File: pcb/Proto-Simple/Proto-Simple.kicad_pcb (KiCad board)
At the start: 2 copper layers, 52 x 63 mm, 341 parts, among them J1 Conn_01x04, J10 Conn_01x01, J11 Conn_01x01, J12 Conn_01x01, J13 Conn_01x01, J14 Conn_01x01, J2 Conn_01x01, J3 Conn_01x01, J4 Conn_01x01, J41 Conn_01x01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

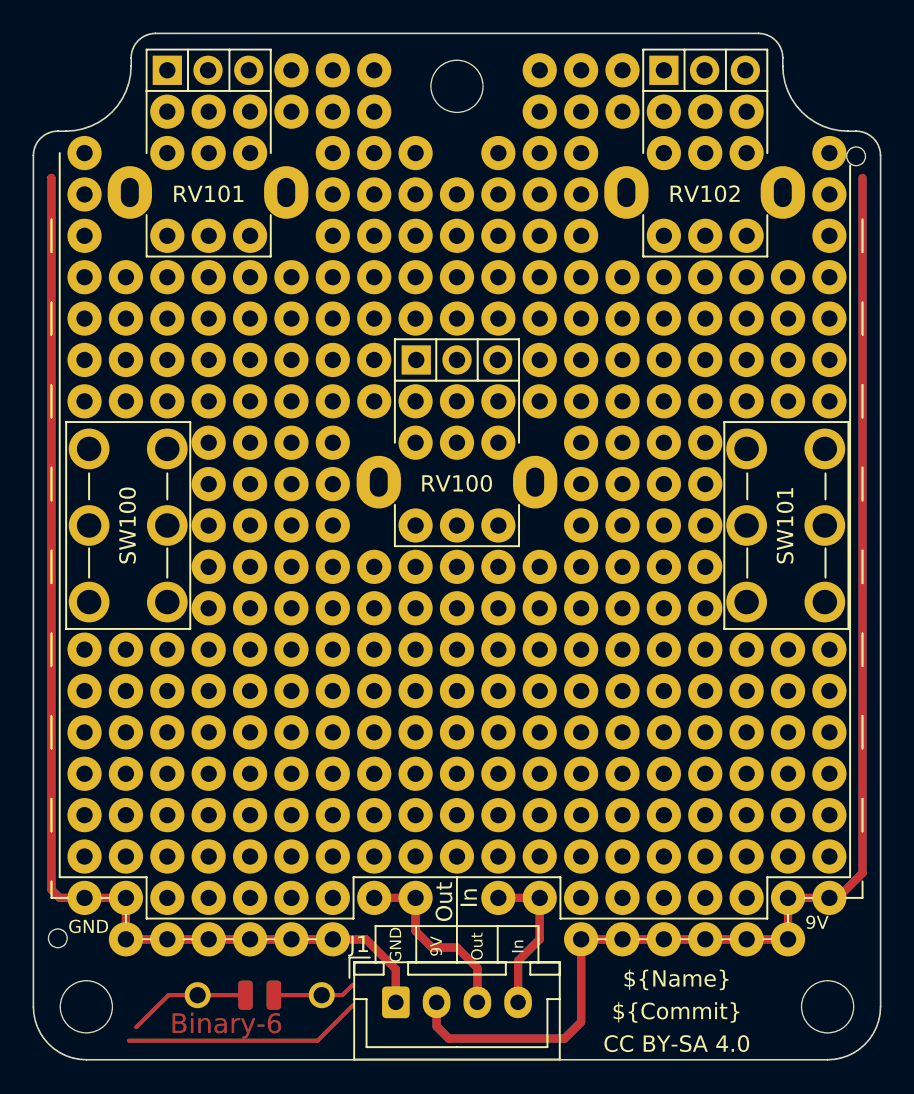
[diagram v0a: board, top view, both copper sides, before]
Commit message: [ProtoAdvanced][ProtoSimple] Make power rails wider
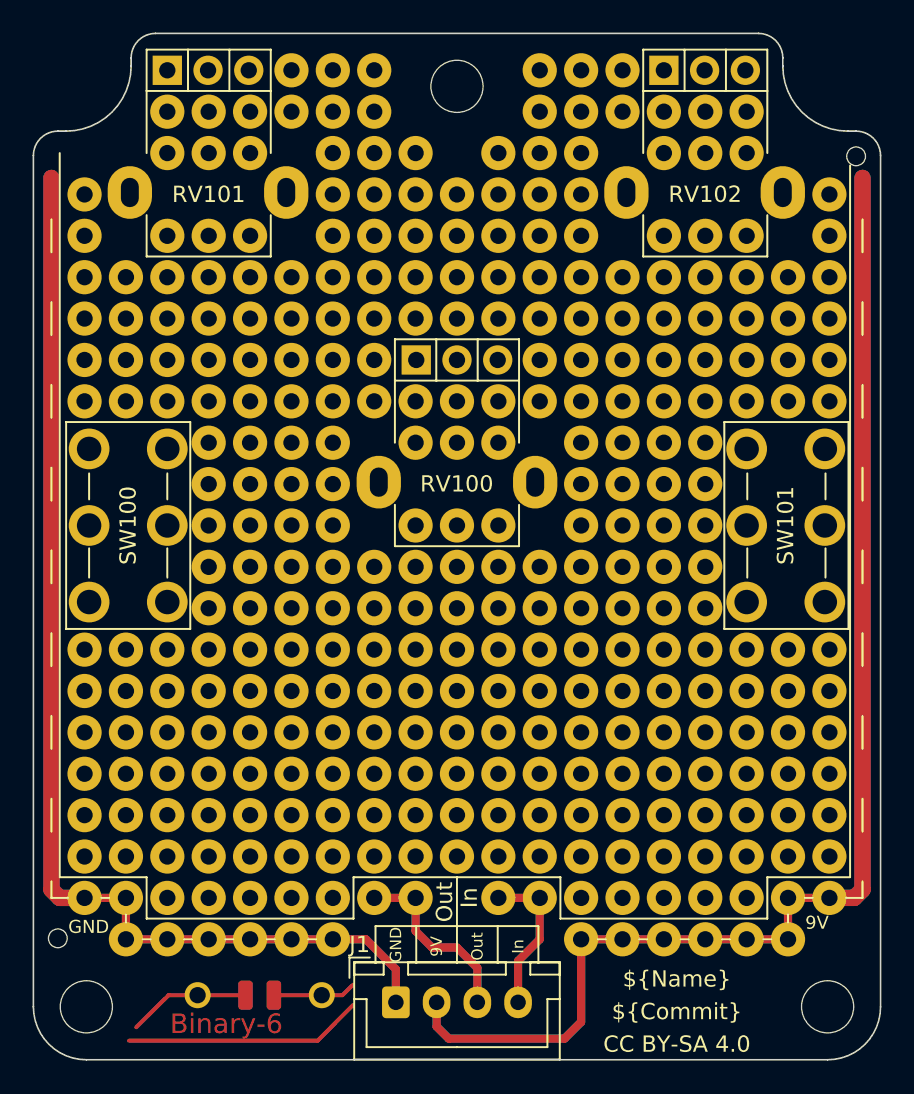
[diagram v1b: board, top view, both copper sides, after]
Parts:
- removed the REF** at (126.6, 74.8)
- removed the REF** at (172.4, 74.8)
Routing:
- net +9V: track 158.6 -> 159.7 mm

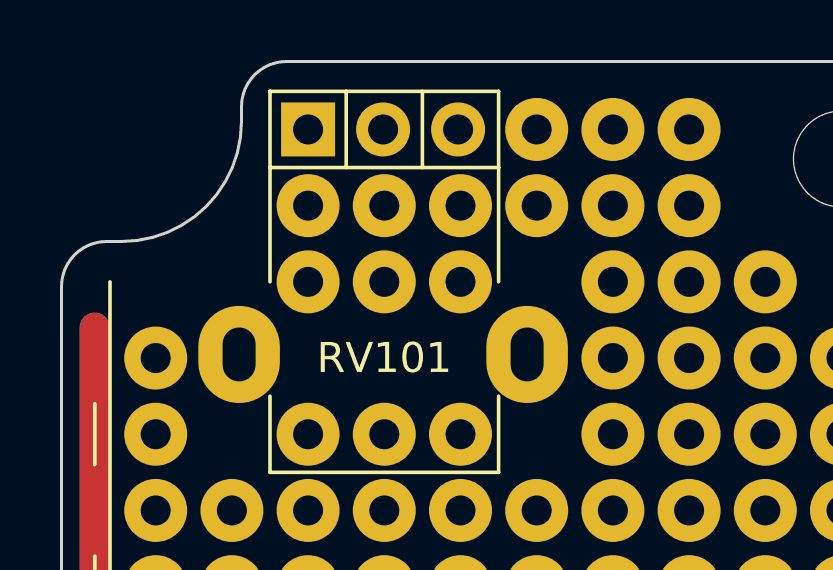
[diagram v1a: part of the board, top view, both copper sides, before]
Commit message: [All] Update all pot footprints and silkscreens
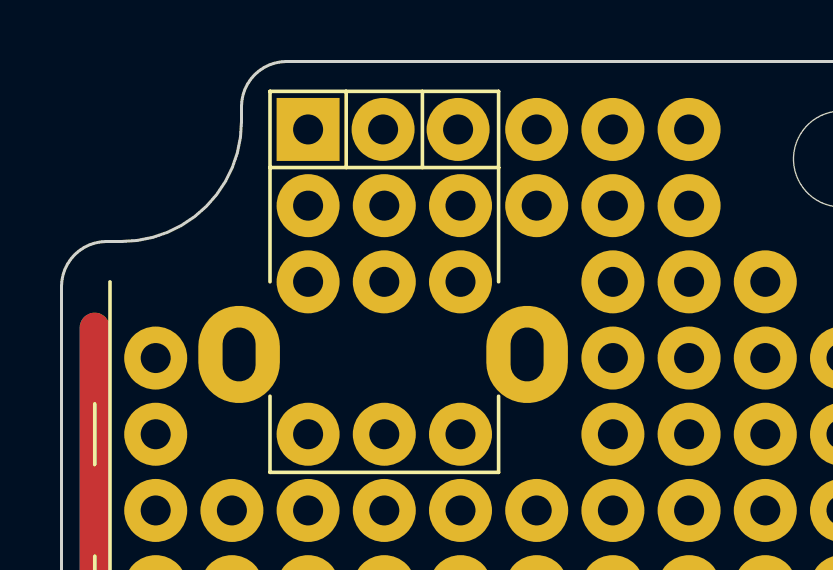
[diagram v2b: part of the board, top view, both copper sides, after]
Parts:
- RV101: footprint Potentiometer_THT:Potentiometer_Alpha_RD901F-40-00D_Single_Vertical -> MeineBib:Potentiometer_Alpha_RD901F-40-00D_Single_Vertical
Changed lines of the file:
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@@
     )
   )
-  (footprint "Potentiometer_THT:Potentiometer_Alpha_RD901F-40-00D_Single_Vertical" (layer "B.Cu")
+  (footprint "MeineBib:Potentiometer_Alpha_RD901F-40-00D_Single_Vertical" (layer "B.Cu")
     (at 131.72 69.765 -90)
     (descr "Potentiometer, vertical, 9mm, single, http://www.taiwanalpha.com.tw/downloads?target=products&id=113")
@@
     (property "Sheetname" "")
     (attr through_hole)
-    (fp_text reference "RV101" (at 7.62 -2.54 180) (layer "B.SilkS")
+    (fp_text reference "RV101" (at 7.493 -2.413 180) (layer "B.SilkS")
       (effects (font (size 1 1) (thickness 0.15)) (justify mirror))
     )
-    (fp_text value "100K Lin" (at 2.54 -2.5 180) (layer "B.Fab")
+    (fp_text value "100K Lin" (at 0 -9.86 90) (layer "B.Fab")
       (effects (font (size 1 1) (thickness 0.15)) (justify mirror))
-    )
-    (fp_text user "${REFERENCE}" (at 7.62 -2.54 180) (layer "F.SilkS")
-      (effects (font (size 1 1) (thickness 0.15)))
     )
     (fp_text user "${REFERENCE}" (at 7.62 -2.54 90) (layer "B.Fab")
       (effects (font (size 1 1) (thickness 0.15)) (justify mirror))
     )
+    (fp_line (start -1.15 3.91) (end -1.15 -8.91) (layer "B.CrtYd") (width 0.05))
     (fp_line (start -1.15 -8.91) (end 12.6 -8.91) (layer "B.CrtYd") (width 0.05))
+    (fp_line (start 12.6 -8.91) (end 12.6 3.91) (layer "B.CrtYd") (width 0.05))
     (fp_line (start 12.6 3.91) (end -1.15 3.91) (layer "B.CrtYd") (width 0.05))
-    (fp_line (start -1.15 3.91) (end -1.15 -8.91) (layer "B.CrtYd") (width 0.05))
-    (fp_line (start 12.6 -8.91) (end 12.6 3.91) (layer "B.CrtYd") (width 0.05))
+    (fp_line (start 1 -7.25) (end 1 2.25) (layer "B.Fab") (width 0.1))
+    (fp_line (start 1 2.25) (end 12.35 2.25) (layer "B.Fab") (width 0.1))
+    (fp_line (start 12.35 -7.25) (end 12.35 2.25) (layer "B.Fab") (width 0.1))
     (fp_line (start 1 -7.25) (end 12.35 -7.25) (layer "B.Fab") (width 0.1))
-    (fp_line (start 1 2.25) (end 12.35 2.25) (layer "B.Fab") (width 0.1))
-    (fp_line (start 1 -7.25) (end 1 2.25) (layer "B.Fab") (width 0.1))
-    (fp_line (start 12.35 -7.25) (end 12.35 2.25) (layer "B.Fab") (width 0.1))
     (fp_circle (center 7.5 -2.5) (end 7.5 1) (layer "B.Fab") (width 0.1) (fill none))
+    (pad "" thru_hole oval (at 7.5 2.3 180) (size 2.72 3.24) (drill oval 1.1 1.8) (layers *.Cu *.Mask))
     (pad "" thru_hole oval (at 7.5 -7.3 180) (size 2.72 3.24) (drill oval 1.1 1.8) (layers *.Cu *.Mask))
-    (pad "" thru_hole oval (at 7.5 2.3 180) (size 2.72 3.24) (drill oval 1.1 1.8) (layers *.Cu *.Mask))
-    (pad "1" thru_hole rect (at 0 0 180) (size 1.8 1.8) (drill 1) (layers *.Cu *.Mask)
+    (pad "1" thru_hole rect (at 0 0 180) (size 2.1 2.1) (drill 1) (layers *.Cu *.Mask)
       (net 8 "unconnected-(RV101-Pad1)") (pinfunction "1") (pintype "passive"))
-    (pad "2" thru_hole circle (at 0 -2.5 180) (size 1.8 1.8) (drill 1) (layers *.Cu *.Mask)
+    (pad "2" thru_hole circle (at 0 -2.5 180) (size 2.1 2.1) (drill 1) (layers *.Cu *.Mask)
       (net 9 "unconnected-(RV101-Pad2)") (pinfunction "2") (pintype "passive"))
-    (pad "3" thru_hole circle (at 0 -5 180) (size 1.8 1.8) (drill 1) (layers *.Cu *.Mask)
+    (pad "3" thru_hole circle (at 0 -5 180) (size 2.1 2.1) (drill 1) (layers *.Cu *.Mask)
       (net 10 "unconnected-(RV101-Pad3)") (pinfunction "3") (pintype "passive"))
     (model "${MEINE_BIBS}/MeineBib.3dshapes/alpha_pot_RD901F-40-15R1.step"
@@
       (rotate (xyz 0 0 90))
     )
-    (model "${MEINE_BIBS}/MeineBib.3dshapes/PotKnob.wrl"
-      (offset (xyz 7.5 -2.5 0.6))
+    (model "${MEINE_BIBS}/MeineBib.3dshapes/PotKnob.step"
+      (offset (xyz 7.5 -2.5 0))
       (scale (xyz 1 1 1))
       (rotate (xyz 0 0 90))
@@
   (gr_line (start 130.45 119.295) (end 130.45 121.835) (layer "B.SilkS") (width 0.12))
   (gr_line (start 130.45 68.495) (end 138.07 68.495) (layer "B.SilkS") (width 0.12))
-  (gr_line (start 123.706 104.055) (end 123.706 91.355) (layer "B.SilkS") (width 0.12))
   (gr_line (start 152 124.5582) (end 152 122.2922) (layer "B.SilkS") (width 0.12))
   (gr_line (start 132.736 123.105) (end 133.244 123.105) (layer "B.SilkS") (width 0.12))

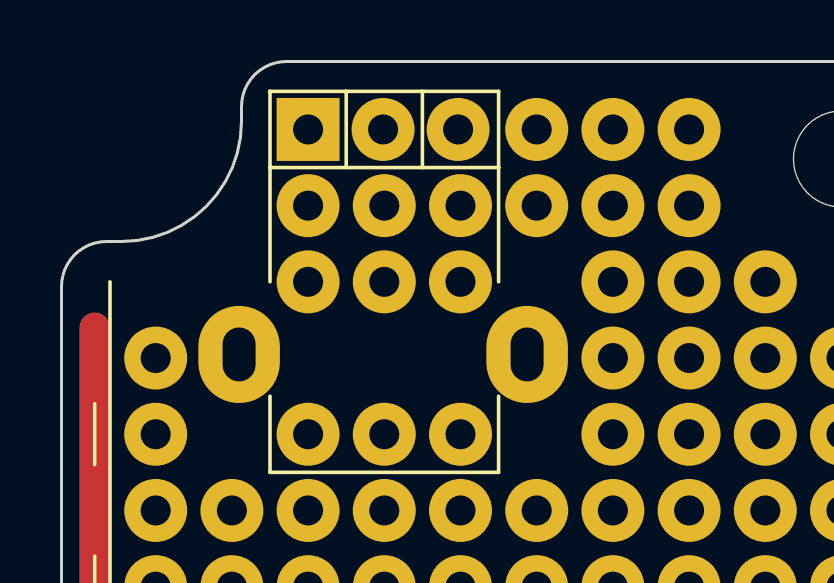
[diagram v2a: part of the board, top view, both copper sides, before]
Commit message: [All] Find out that the upper left pot is 0,08mm off on all designs
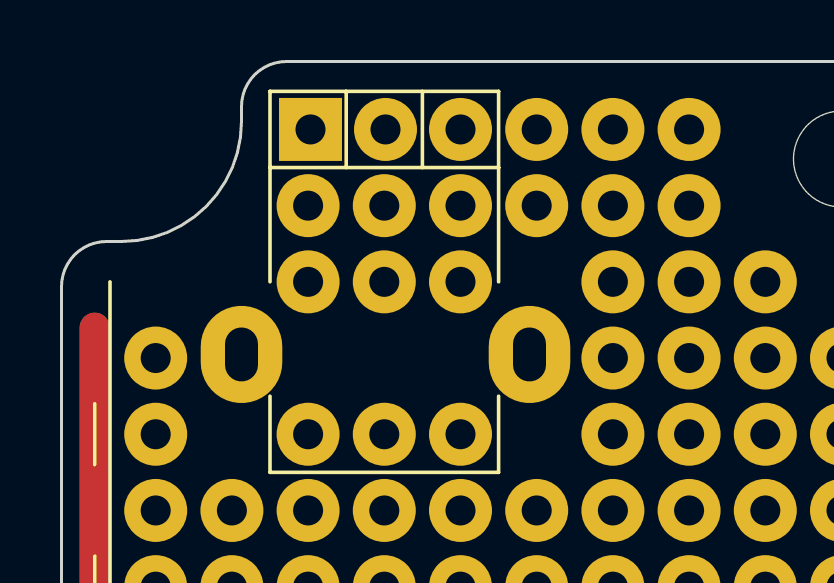
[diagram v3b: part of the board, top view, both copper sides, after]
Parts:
- moved RV101 0.08 mm to (131.8, 69.8)
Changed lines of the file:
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@@
   )
   (footprint "MeineBib:Potentiometer_Alpha_RD901F-40-00D_Single_Vertical" (layer "B.Cu")
-    (at 131.72 69.765 -90)
+    (at 131.8 69.765 -90)
     (descr "Potentiometer, vertical, 9mm, single, http://www.taiwanalpha.com.tw/downloads?target=products&id=113")
     (tags "potentiometer vertical 9mm single")
